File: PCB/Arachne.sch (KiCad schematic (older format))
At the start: 38 parts, among them SW101 SW_Push, U101 STM32L452CEUx, U102 WS2818B

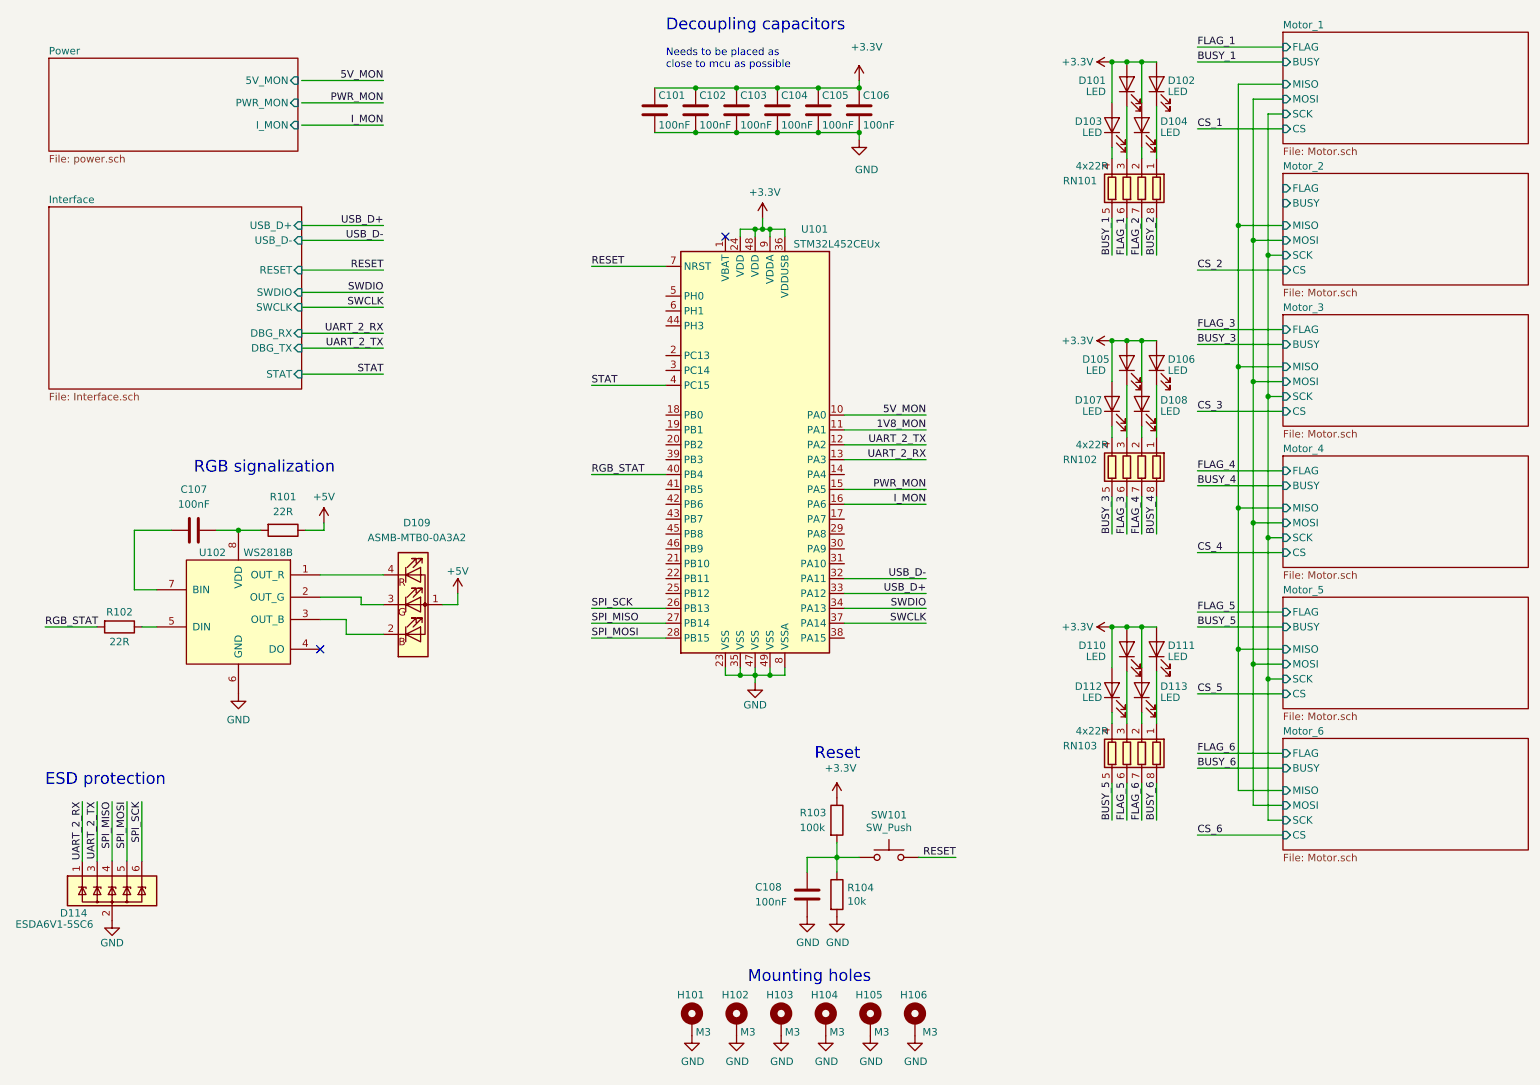
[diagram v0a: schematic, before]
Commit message: Schema: fix schema ERC, connect CS, FLAG and BUSY pins to MCU, connect SPI
ERC: fixed L6470 pin types, add power flags, fixed programming
connector pin types
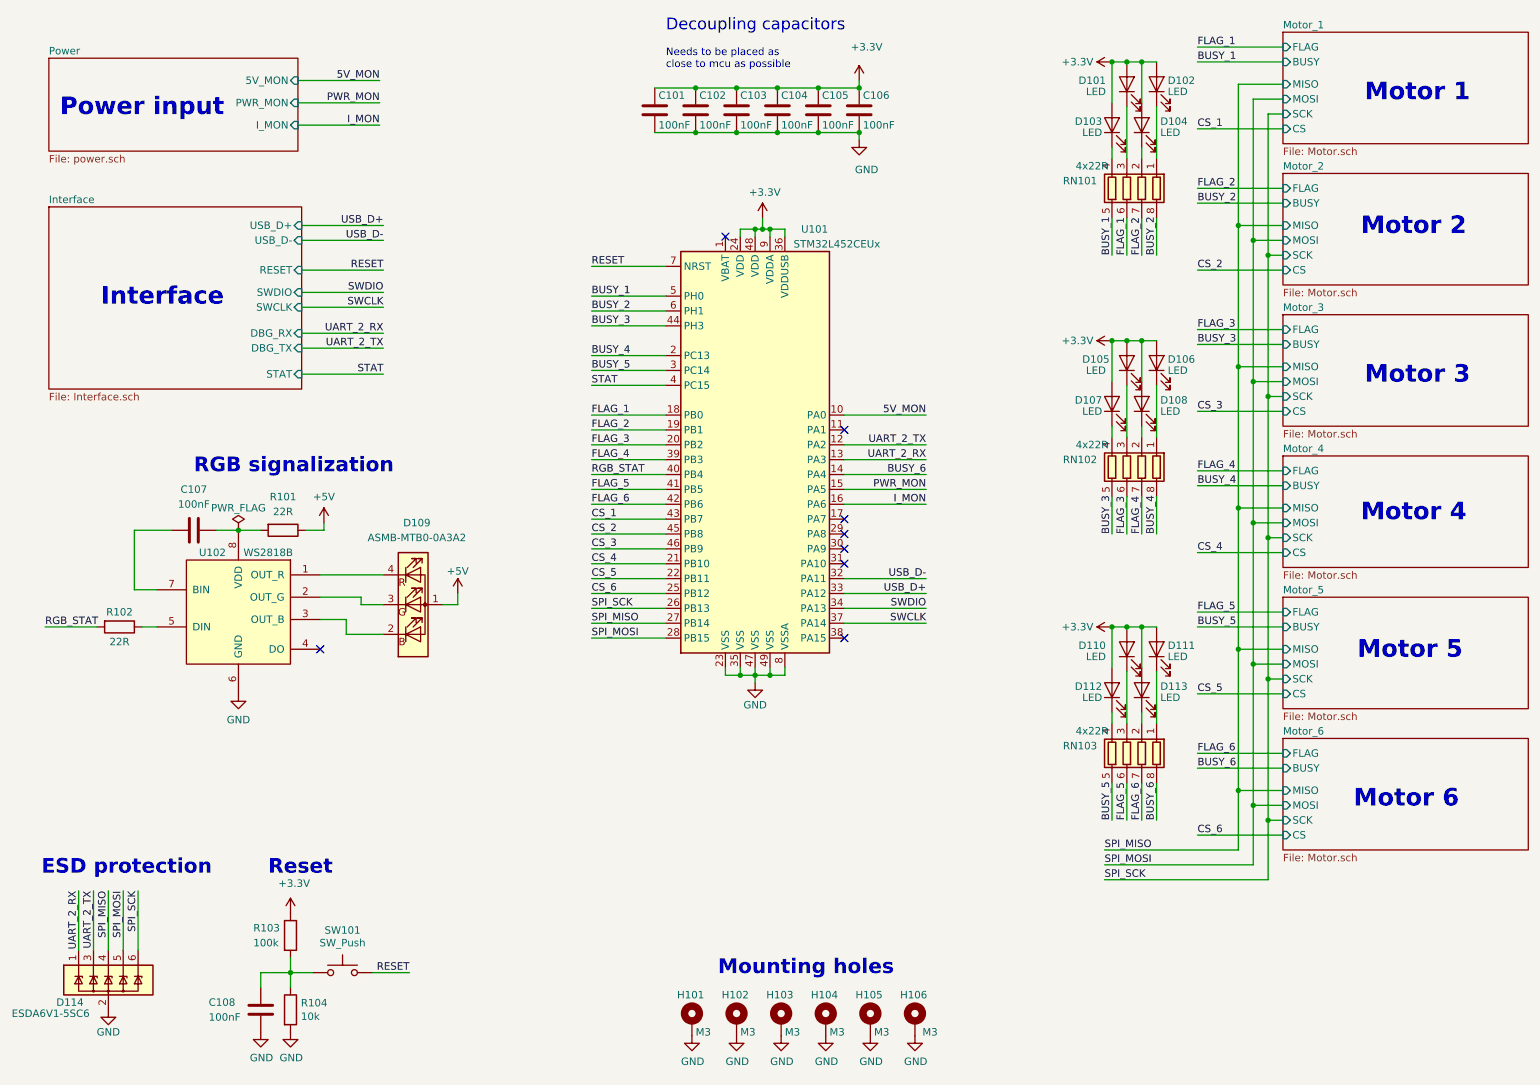
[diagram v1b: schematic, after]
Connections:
- net BUSY_1: now also U101.5 (PH0)
- net BUSY_2: now also U101.6 (PH1)
- net BUSY_3: now also U101.44 (PH3)
- net BUSY_4: now also U101.2 (PC13)
- net BUSY_5: now also U101.3 (PC14)
- net BUSY_6: now also U101.14 (PA4)
- net CS_1: now also U101.43 (PB7)
- net CS_2: now also U101.45 (PB8)
- net CS_3: now also U101.46 (PB9)
- net CS_4: now also U101.21 (PB10)
- net CS_5: now also U101.22 (PB11)
- net CS_6: now also U101.25 (PB12)
- net FLAG_1: now also U101.18 (PB0)
- net FLAG_2: now also U101.19 (PB1)
- net FLAG_3: now also U101.20 (PB2)
- net FLAG_4: now also U101.39 (PB3)
- net FLAG_5: now also U101.41 (PB5)
- net FLAG_6: now also U101.42 (PB6)
- net 1V8_MON: no longer names the net of U101.11 (PA1)
- no-connect marks 2 -> 8
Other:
- note added: "Interface"
- note added: "Motor 1"
- note added: "Motor 2\n"
- note added: "Motor 3"
- note added: "Motor 4\n"
- note added: "Motor 5"
- note added: "Motor 6\n"
- note added: "Power input"
- moved on the sheet: C108, D114, R103, R104, SW101

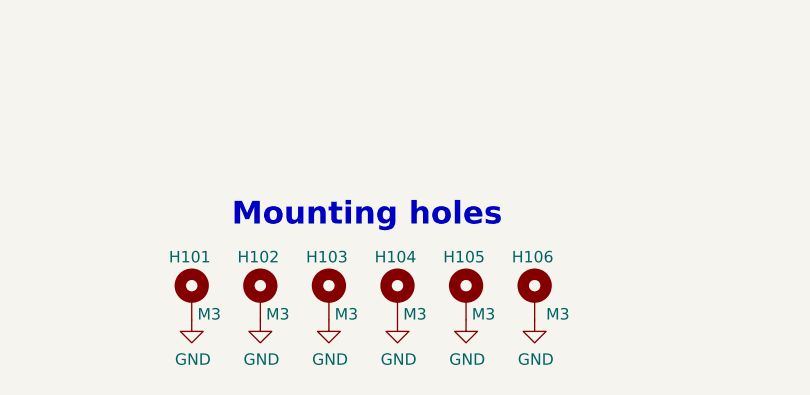
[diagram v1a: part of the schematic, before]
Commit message: Schema&PCB: shrink board to 80x100mm, remove excessive mounting holes
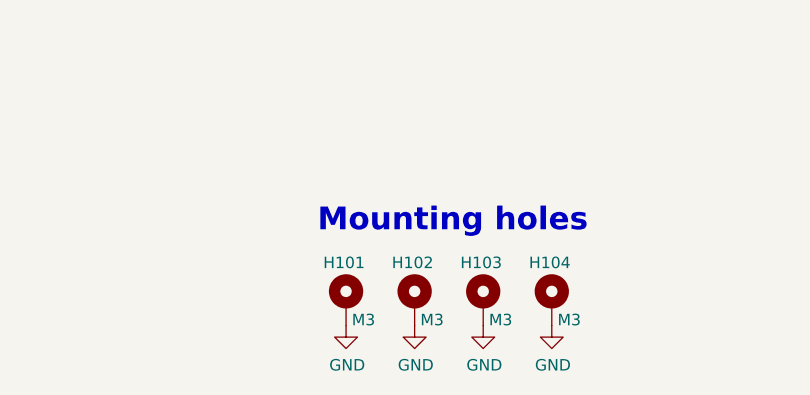
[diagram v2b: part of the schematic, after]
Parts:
- removed H105, H106: M3, MountingHole:MountingHole_3.2mm_M3_Pad_Via, symbol Mechanical:MountingHole_Pad
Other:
- moved on the sheet: H101, H102, H103, H104
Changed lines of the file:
@@
-$Comp
-L Mechanical:MountingHole_Pad H?
-U 1 1 5E45EF92
-P 6375 7350
-AR Path="/5E44BE52/5E45EF92" Ref="H?"  Part="1"
-AR Path="/5E45EF92" Ref="H105"  Part="1"
-F 0 "H105" H 6275 7525 50  0000 L CNN
-F 1 "M3" H 6400 7275 50  0000 L CNN
-F 2 "MountingHole:MountingHole_3.2mm_M3_Pad_Via" H 6375 7350 50  0001 C CNN
-F 3 "~" H 6375 7350 50  0001 C CNN
-	1    6375 7350
-	1    0    0    -1
-$EndComp
-$Comp
-L power:GND #PWR?
-U 1 1 5E45EF98
-P 6375 7450
-AR Path="/5E44BE52/5E45EF98" Ref="#PWR?"  Part="1"
-AR Path="/5E45EF98" Ref="#PWR0119"  Part="1"
-F 0 "#PWR0119" H 6375 7200 50  0001 C CNN
-F 1 "GND" H 6380 7277 50  0000 C CNN
-F 2 "" H 6375 7450 50  0001 C CNN
-F 3 "" H 6375 7450 50  0001 C CNN
-	1    6375 7450
-	1    0    0    -1
-$EndComp
 $Comp
 L Mechanical:MountingHole_Pad H?
 U 1 1 5E45EF9E
-P 6075 7350
+P 6750 7375
 AR Path="/5E44BE52/5E45EF9E" Ref="H?"  Part="1"
 AR Path="/5E45EF9E" Ref="H104"  Part="1"
-F 0 "H104" H 5975 7525 50  0000 L CNN
-F 1 "M3" H 6100 7275 50  0000 L CNN
-F 2 "MountingHole:MountingHole_3.2mm_M3_Pad_Via" H 6075 7350 50  0001 C CNN
-F 3 "~" H 6075 7350 50  0001 C CNN
-	1    6075 7350
+F 0 "H104" H 6650 7550 50  0000 L CNN
+F 1 "M3" H 6775 7300 50  0000 L CNN
+F 2 "MountingHole:MountingHole_3.2mm_M3_Pad_Via" H 6750 7375 50  0001 C CNN
+F 3 "~" H 6750 7375 50  0001 C CNN
+	1    6750 7375
 	1    0    0    -1
 $EndComp
@@
 L power:GND #PWR?
 U 1 1 5E45EFA4
-P 6075 7450
+P 6750 7475
 AR Path="/5E44BE52/5E45EFA4" Ref="#PWR?"  Part="1"
 AR Path="/5E45EFA4" Ref="#PWR0118"  Part="1"
-F 0 "#PWR0118" H 6075 7200 50  0001 C CNN
-F 1 "GND" H 6080 7277 50  0000 C CNN
-F 2 "" H 6075 7450 50  0001 C CNN
-F 3 "" H 6075 7450 50  0001 C CNN
-	1    6075 7450
+F 0 "#PWR0118" H 6750 7225 50  0001 C CNN
+F 1 "GND" H 6755 7302 50  0000 C CNN
+F 2 "" H 6750 7475 50  0001 C CNN
+F 3 "" H 6750 7475 50  0001 C CNN
+	1    6750 7475
 	1    0    0    -1
 $EndComp
@@
 L Mechanical:MountingHole_Pad H?
 U 1 1 5E45EFAA
-P 5475 7350
+P 6150 7375
 AR Path="/5E44BE52/5E45EFAA" Ref="H?"  Part="1"
 AR Path="/5E45EFAA" Ref="H102"  Part="1"
-F 0 "H102" H 5375 7525 50  0000 L CNN
-F 1 "M3" H 5500 7275 50  0000 L CNN
-F 2 "MountingHole:MountingHole_3.2mm_M3_Pad_Via" H 5475 7350 50  0001 C CNN
-F 3 "~" H 5475 7350 50  0001 C CNN
-	1    5475 7350
+F 0 "H102" H 6050 7550 50  0000 L CNN
+F 1 "M3" H 6175 7300 50  0000 L CNN
+F 2 "MountingHole:MountingHole_3.2mm_M3_Pad_Via" H 6150 7375 50  0001 C CNN
+F 3 "~" H 6150 7375 50  0001 C CNN
+	1    6150 7375
 	1    0    0    -1
 $EndComp
@@
 L Mechanical:MountingHole_Pad H?
 U 1 1 5E45EFB0
-P 5775 7350
+P 6450 7375
 AR Path="/5E44BE52/5E45EFB0" Ref="H?"  Part="1"
 AR Path="/5E45EFB0" Ref="H103"  Part="1"
-F 0 "H103" H 5675 7525 50  0000 L CNN
-F 1 "M3" H 5800 7275 50  0000 L CNN
-F 2 "MountingHole:MountingHole_3.2mm_M3_Pad_Via" H 5775 7350 50  0001 C CNN
-F 3 "~" H 5775 7350 50  0001 C CNN
-	1    5775 7350
+F 0 "H103" H 6350 7550 50  0000 L CNN
+F 1 "M3" H 6475 7300 50  0000 L CNN
+F 2 "MountingHole:MountingHole_3.2mm_M3_Pad_Via" H 6450 7375 50  0001 C CNN
+F 3 "~" H 6450 7375 50  0001 C CNN
+	1    6450 7375
 	1    0    0    -1
 $EndComp
@@
 L power:GND #PWR?
 U 1 1 5E45EFB6
-P 5475 7450
+P 6150 7475
 AR Path="/5E44BE52/5E45EFB6" Ref="#PWR?"  Part="1"
 AR Path="/5E45EFB6" Ref="#PWR0116"  Part="1"
-F 0 "#PWR0116" H 5475 7200 50  0001 C CNN
-F 1 "GND" H 5480 7277 50  0000 C CNN
-F 2 "" H 5475 7450 50  0001 C CNN
-F 3 "" H 5475 7450 50  0001 C CNN
-	1    5475 7450
+F 0 "#PWR0116" H 6150 7225 50  0001 C CNN
+F 1 "GND" H 6155 7302 50  0000 C CNN
+F 2 "" H 6150 7475 50  0001 C CNN
+F 3 "" H 6150 7475 50  0001 C CNN
+	1    6150 7475
 	1    0    0    -1
 $EndComp
@@
 L power:GND #PWR?
 U 1 1 5E45EFBC
-P 5775 7450
+P 6450 7475
 AR Path="/5E44BE52/5E45EFBC" Ref="#PWR?"  Part="1"
 AR Path="/5E45EFBC" Ref="#PWR0117"  Part="1"
-F 0 "#PWR0117" H 5775 7200 50  0001 C CNN
-F 1 "GND" H 5780 7277 50  0000 C CNN
-F 2 "" H 5775 7450 50  0001 C CNN
-F 3 "" H 5775 7450 50  0001 C CNN
-	1    5775 7450
+F 0 "#PWR0117" H 6450 7225 50  0001 C CNN
+F 1 "GND" H 6455 7302 50  0000 C CNN
+F 2 "" H 6450 7475 50  0001 C CNN
+F 3 "" H 6450 7475 50  0001 C CNN
+	1    6450 7475
 	1    0    0    -1
 $EndComp
@@
 L Mechanical:MountingHole_Pad H?
 U 1 1 5E45EFC2
-P 5175 7350
+P 5850 7375
 AR Path="/5E44BE52/5E45EFC2" Ref="H?"  Part="1"
 AR Path="/5E45EFC2" Ref="H101"  Part="1"
-F 0 "H101" H 5075 7525 50  0000 L CNN
-F 1 "M3" H 5200 7275 50  0000 L CNN
-F 2 "MountingHole:MountingHole_3.2mm_M3_Pad_Via" H 5175 7350 50  0001 C CNN
-F 3 "~" H 5175 7350 50  0001 C CNN
-	1    5175 7350
+F 0 "H101" H 5750 7550 50  0000 L CNN
+F 1 "M3" H 5875 7300 50  0000 L CNN
+F 2 "MountingHole:MountingHole_3.2mm_M3_Pad_Via" H 5850 7375 50  0001 C CNN
+F 3 "~" H 5850 7375 50  0001 C CNN
+	1    5850 7375
 	1    0    0    -1
 $EndComp
@@
 L power:GND #PWR?
 U 1 1 5E45EFC8
-P 5175 7450
+P 5850 7475
 AR Path="/5E44BE52/5E45EFC8" Ref="#PWR?"  Part="1"
 AR Path="/5E45EFC8" Ref="#PWR0115"  Part="1"
-F 0 "#PWR0115" H 5175 7200 50  0001 C CNN
-F 1 "GND" H 5180 7277 50  0000 C CNN
-F 2 "" H 5175 7450 50  0001 C CNN
-F 3 "" H 5175 7450 50  0001 C CNN
-	1    5175 7450
+F 0 "#PWR0115" H 5850 7225 50  0001 C CNN
+F 1 "GND" H 5855 7302 50  0000 C CNN
+F 2 "" H 5850 7475 50  0001 C CNN
+F 3 "" H 5850 7475 50  0001 C CNN
+	1    5850 7475
 	1    0    0    -1
 $EndComp
-Text Notes 5350 7050 0    99   ~ 20
+Text Notes 5725 7075 0    99   ~ 20
 Mounting holes
 $Comp
@@
 Reset
 $Comp
-L Mechanical:MountingHole_Pad H?
-U 1 1 5E45EFEA
-P 6675 7350
-AR Path="/5E44BE52/5E45EFEA" Ref="H?"  Part="1"
-AR Path="/5E45EFEA" Ref="H106"  Part="1"
-F 0 "H106" H 6575 7525 50  0000 L CNN
-F 1 "M3" H 6725 7275 50  0000 L CNN
-F 2 "MountingHole:MountingHole_3.2mm_M3_Pad_Via" H 6675 7350 50  0001 C CNN
-F 3 "~" H 6675 7350 50  0001 C CNN
-	1    6675 7350
-	1    0    0    -1
-$EndComp
-$Comp
-L power:GND #PWR?
-U 1 1 5E45EFF0
-P 6675 7450
-AR Path="/5E44BE52/5E45EFF0" Ref="#PWR?"  Part="1"
-AR Path="/5E45EFF0" Ref="#PWR0120"  Part="1"
-F 0 "#PWR0120" H 6675 7200 50  0001 C CNN
-F 1 "GND" H 6680 7277 50  0000 C CNN
-F 2 "" H 6675 7450 50  0001 C CNN
-F 3 "" H 6675 7450 50  0001 C CNN
-	1    6675 7450
-	1    0    0    -1
-$EndComp
-$Comp
 L power:+3.3V #PWR?
